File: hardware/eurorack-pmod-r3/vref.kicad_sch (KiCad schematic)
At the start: 6 parts, among them U8 LM4040DBZ-3, U9 TL072

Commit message: rev3/schematic: add PN and footprint for most components
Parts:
- C26: lcsc# (none) -> C110055; mfg# T491A106K020AT -> T491A106K016AT
- C27: lcsc# (none) -> C338036; mfg# (none) -> C1608X7R1E104KT000N
- R33: renamed from R25; lcsc# (none) -> C105881; mfg# (none) -> RC0603FR-07330RL
- RN7: renamed from RN9; footprint Resistor_SMD:R_Cat16-4 -> Resistor_SMD:R_Array_Convex_4x0402; dig# CAT16-1003F4LFCT-ND -> (none); lcsc# (none) -> C326786; mfg# CAT16-1003F4LF -> YC124-FR-07100KL
- U8: dig# 296-LM4040CEM3X-3.0/NOPBCT-ND -> LM4040BIM3-3.0/NOPB; lcsc# (none) -> C139380; mfg# LM4040CEM3X-3.0/NOPB -> LM4040BIM3-3.0/NOPB
- U9: footprint Package_SO:TSSOP-8_4.4x3mm_P0.65mm -> Package_SO:SOIC-8_3.9x4.9mm_P1.27mm; dig# 296-TL072HIPWRCT-ND -> 497-2200-1-ND; lcsc# (none) -> C6961; mfg# TL072HIPWR -> TL072CDT

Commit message: rev3/pcb: preliminary fab outputs and text labels
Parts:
- C26: value 10u -> 10.0uF
- C27: value 100n -> 100nF
- U8: value LM4040DBZ-3 -> LM4040DBZ-3 VREF
- U9: value TL072 -> TL072 OP AMP
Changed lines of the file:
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@@
       (effects (font (size 1.27 1.27)) (justify right))
     )
-    (property "Value" "LM4040DBZ-3" (id 1) (at 100.0252 45.7453 90)
+    (property "Value" "LM4040DBZ-3 VREF" (id 1) (at 100.0252 45.7453 90)
       (effects (font (size 1.27 1.27)) (justify right))
     )
@@
     (in_bom yes) (on_board yes)
     (property "Reference" "U9" (id 0) (at 165.7604 62.865 0))
-    (property "Value" "TL072" (id 1) (at 165.7604 53.34 0))
+    (property "Value" "TL072 OP AMP" (id 1) (at 165.7604 53.34 0))
     (property "Footprint" "Package_SO:SOIC-8_3.9x4.9mm_P1.27mm" (id 2) (at 165.7604 58.42 0)
       (effects (font (size 1.27 1.27)) hide)
@@
     (in_bom yes) (on_board yes)
     (property "Reference" "U9" (id 0) (at 139.0904 60.325 0))
-    (property "Value" "TL072" (id 1) (at 139.0904 50.8 0))
+    (property "Value" "TL072 OP AMP" (id 1) (at 139.0904 50.8 0))
     (property "Footprint" "Package_SO:SOIC-8_3.9x4.9mm_P1.27mm" (id 2) (at 139.0904 55.88 0)
       (effects (font (size 1.27 1.27)) hide)
@@
       (effects (font (size 1.27 1.27)) (justify left))
     )
-    (property "Value" "100n" (id 1) (at 87.3252 46.3866 0)
+    (property "Value" "100nF" (id 1) (at 87.3252 46.3866 0)
       (effects (font (size 1.27 1.27)) (justify left))
     )
@@
     (in_bom yes) (on_board yes)
     (property "Reference" "C26" (id 0) (at 78.4352 42.5704 0))
-    (property "Value" "10u" (id 1) (at 77.1652 45.1104 0))
+    (property "Value" "10.0uF" (id 1) (at 77.1652 45.1104 0))
     (property "Footprint" "Capacitor_Tantalum_SMD:CP_EIA-3216-10_Kemet-I" (id 2) (at 80.9752 45.1104 0)
       (effects (font (size 1.27 1.27)) hide)
@@
       (effects (font (size 1.27 1.27)) (justify right))
     )
-    (property "Value" "TL072" (id 1) (at 212.09 52.8321 0)
-      (effects (font (size 1.27 1.27)) (justify right))
-    )
+    (property "Value" "TL072 OP AMP" (id 1) (at 212.09 52.8321 0)
+      (effects (font (size 1.27 1.27)) (justify right))
+    )

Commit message: try routing with capsense groundfix
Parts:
- added R36 (x2): X.X, Resistor_SMD:R_0402_1005Metric, symbol Device:R
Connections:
- net +3V0_AREF: now also R36.2
- net GND: now also R36.1
- net at RN7.1 (R1.1), RN7.2 (R2.1): now also R36.1, R36.2; no longer U9.3 (+)
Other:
- note added: "VCOM ADJUST"
- note added: "~1.5V"
- note removed: "+1.5V"
- moved on the sheet: C27, RN7A, RN7B

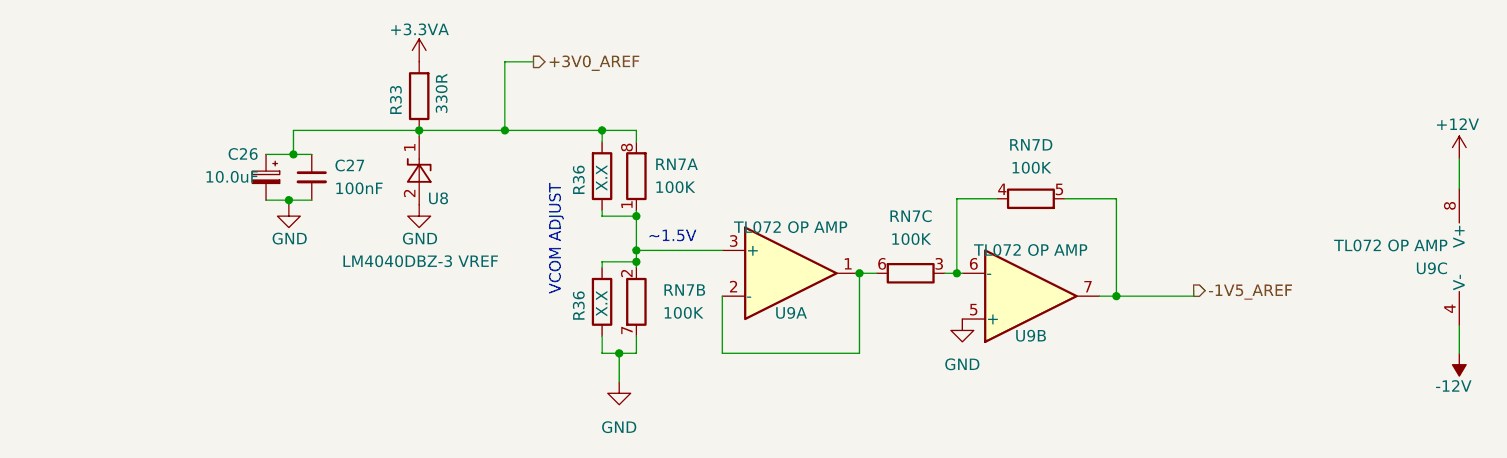
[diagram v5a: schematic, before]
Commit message: Place everything on board, fix some bugs
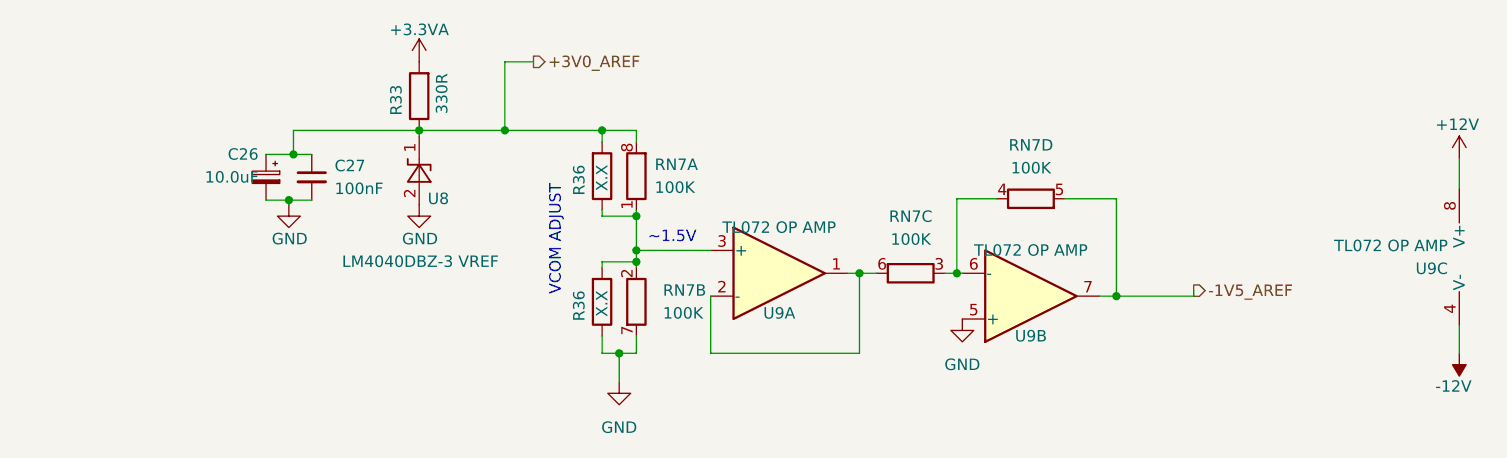
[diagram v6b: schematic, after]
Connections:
- net at R36.1, R36.2, RN7.1 (R1.1)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: now also U9.3 (+)
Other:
- moved on the sheet: U9A
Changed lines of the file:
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@@
+    (stroke (width 0) (type default))
+  )
+  (wire (pts (xy 107.315 32.385) (xy 107.315 40.005))
+    (stroke (width 0) (type default))
+  )
+  (wire (pts (xy 175.26 58.42) (xy 183.8452 58.42))
+    (stroke (width 0) (type default))
+  )
+  (wire (pts (xy 146.7104 64.77) (xy 146.7104 55.88))
+    (stroke (width 0) (type default))
+  )
+  (wire (pts (xy 118.11 41.275) (xy 118.11 40.005))
+    (stroke (width 0) (type default))
+  )
+  (wire (pts (xy 146.7104 55.88) (xy 148.59 55.88))
+    (stroke (width 0) (type default))
+  )
+  (wire (pts (xy 213.36 43.18) (xy 213.36 46.482))
+    (stroke (width 0) (type default))
+  )
+  (wire (pts (xy 118.11 62.865) (xy 118.11 64.77))
+    (stroke (width 0) (type default))
+  )
+  (wire (pts (xy 83.82 40.005) (xy 83.82 42.672))
+    (stroke (width 0) (type default))
+  )
+  (wire (pts (xy 118.11 64.77) (xy 120.015 64.77))
+    (stroke (width 0) (type default))
+  )
+  (wire (pts (xy 97.79 40.005) (xy 97.79 40.64))
+    (stroke (width 0) (type default))
+  )
+  (wire (pts (xy 83.312 47.752) (xy 85.852 47.752))
+    (stroke (width 0) (type default))
+  )
+  (wire (pts (xy 118.11 48.895) (xy 118.11 49.53))
+    (stroke (width 0) (type default))
+  )
+  (wire (pts (xy 107.315 40.005) (xy 118.11 40.005))
+    (stroke (width 0) (type default))
+  )
+  (wire (pts (xy 130.175 64.77) (xy 146.7104 64.77))
+    (stroke (width 0) (type default))
+  )
+  (wire (pts (xy 121.92 40.005) (xy 121.92 41.275))
+    (stroke (width 0) (type default))
+  )
+  (wire (pts (xy 213.36 61.722) (xy 213.36 64.77))
+    (stroke (width 0) (type default))
+  )
+  (wire (pts (xy 183.8452 57.8104) (xy 183.8452 58.42))
+    (stroke (width 0) (type default))
+  )
+  (wire (pts (xy 118.11 40.005) (xy 121.92 40.005))
+    (stroke (width 0) (type default))
+  )
+  (wire (pts (xy 175.26 47.5996) (xy 175.26 58.42))
+    (stroke (width 0) (type default))
+  )
+  (wire (pts (xy 145.415 55.88) (xy 146.7104 55.88))
+    (stroke (width 0) (type default))
+  )
+  (wire (pts (xy 120.015 64.77) (xy 121.92 64.77))
+    (stroke (width 0) (type default))
+  )
+  (wire (pts (xy 173.3804 58.42) (xy 175.26 58.42))
+    (stroke (width 0) (type default))
+  )
+  (wire (pts (xy 121.92 64.77) (xy 121.92 62.865))
     (stroke (width 0) (type default))
   )
@@
     (stroke (width 0) (type default))
   )
-  (wire (pts (xy 107.315 32.385) (xy 107.315 40.005))
-    (stroke (width 0) (type default))
-  )
-  (wire (pts (xy 175.26 58.42) (xy 183.8452 58.42))
-    (stroke (width 0) (type default))
-  )
-  (wire (pts (xy 146.7104 64.77) (xy 146.7104 55.88))
-    (stroke (width 0) (type default))
-  )
-  (wire (pts (xy 118.11 41.275) (xy 118.11 40.005))
-    (stroke (width 0) (type default))
-  )
-  (wire (pts (xy 146.7104 55.88) (xy 148.59 55.88))
-    (stroke (width 0) (type default))
-  )
-  (wire (pts (xy 213.36 43.18) (xy 213.36 46.482))
-    (stroke (width 0) (type default))
-  )
-  (wire (pts (xy 118.11 62.865) (xy 118.11 64.77))
-    (stroke (width 0) (type default))
-  )
-  (wire (pts (xy 83.82 40.005) (xy 83.82 42.672))
-    (stroke (width 0) (type default))
-  )
-  (wire (pts (xy 118.11 64.77) (xy 120.015 64.77))
-    (stroke (width 0) (type default))
-  )
-  (wire (pts (xy 97.79 40.005) (xy 97.79 40.64))
-    (stroke (width 0) (type default))
-  )
-  (wire (pts (xy 83.312 47.752) (xy 85.852 47.752))
-    (stroke (width 0) (type default))
-  )
-  (wire (pts (xy 118.11 48.895) (xy 118.11 49.53))
-    (stroke (width 0) (type default))
-  )
-  (wire (pts (xy 107.315 40.005) (xy 118.11 40.005))
-    (stroke (width 0) (type default))
-  )
-  (wire (pts (xy 131.4704 64.77) (xy 146.7104 64.77))
-    (stroke (width 0) (type default))
-  )
-  (wire (pts (xy 131.445 53.34) (xy 121.92 53.34))
-    (stroke (width 0) (type default))
-  )
-  (wire (pts (xy 121.92 40.005) (xy 121.92 41.275))
-    (stroke (width 0) (type default))
-  )
-  (wire (pts (xy 213.36 61.722) (xy 213.36 64.77))
-    (stroke (width 0) (type default))
-  )
-  (wire (pts (xy 183.8452 57.8104) (xy 183.8452 58.42))
-    (stroke (width 0) (type default))
-  )
-  (wire (pts (xy 118.11 40.005) (xy 121.92 40.005))
-    (stroke (width 0) (type default))
-  )
-  (wire (pts (xy 175.26 47.5996) (xy 175.26 58.42))
-    (stroke (width 0) (type default))
-  )
-  (wire (pts (xy 120.015 64.77) (xy 121.92 64.77))
-    (stroke (width 0) (type default))
-  )
-  (wire (pts (xy 173.3804 58.42) (xy 175.26 58.42))
-    (stroke (width 0) (type default))
-  )
-  (wire (pts (xy 121.92 64.77) (xy 121.92 62.865))
-    (stroke (width 0) (type default))
-  )
-  (wire (pts (xy 131.4704 58.42) (xy 131.4704 64.77))
+  (wire (pts (xy 130.175 58.42) (xy 130.175 64.77))
     (stroke (width 0) (type default))
   )
@@
     (stroke (width 0) (type default))
   )
+  (wire (pts (xy 121.92 53.34) (xy 130.175 53.34))
+    (stroke (width 0) (type default))
+  )
   (wire (pts (xy 80.772 47.752) (xy 83.312 47.752))
     (stroke (width 0) (type default))
@@
     (stroke (width 0) (type default))
   )
-  (wire (pts (xy 121.92 53.34) (xy 121.92 49.53))
+  (wire (pts (xy 121.92 49.53) (xy 121.92 53.34))
     (stroke (width 0) (type default))
   )
@@
     )
   )
-  (symbol (lib_id "Amplifier_Operational:TL072") (at 139.0904 55.88 0) (unit 1)
-    (in_bom yes) (on_board yes) (dnp no)
-    (property "Reference" "U9" (at 139.0904 60.325 0)
-      (effects (font (size 1.27 1.27)))
-    )
-    (property "Value" "TL072 OP AMP" (at 139.0904 50.8 0)
-      (effects (font (size 1.27 1.27)))
-    )
-    (property "Footprint" "Package_SO:SOIC-8_3.9x4.9mm_P1.27mm" (at 139.0904 55.88 0)
-      (effects (font (size 1.27 1.27)) hide)
-    )
-    (property "Datasheet" "https://www.st.com/content/ccc/resource/technical/document/datasheet/bb/4d/19/24/7d/40/48/a6/CD00000490.pdf/files/CD00000490.pdf/jcr:content/translations/en.CD00000490.pdf" (at 139.0904 55.88 0)
-      (effects (font (size 1.27 1.27)) hide)
-    )
-    (property "dig#" "497-2200-1-ND" (at 139.0904 70.485 0)
-      (effects (font (size 1.27 1.27)) hide)
-    )
-    (property "mfg#" "TL072CDT" (at 139.0904 73.025 0)
-      (effects (font (size 1.27 1.27)) hide)
-    )
-    (property "lcsc#" "C6961" (at 139.0904 55.88 0)
-      (effects (font (size 1.27 1.27)) hide)
-    )
+  (symbol (lib_id "Amplifier_Operational:TL072") (at 137.795 55.88 0) (unit 1)
+    (in_bom yes) (on_board yes) (dnp no)
+    (property "Reference" "U9" (at 137.795 60.325 0)
+      (effects (font (size 1.27 1.27)))
+    )
+    (property "Value" "TL072 OP AMP" (at 137.795 50.8 0)
+      (effects (font (size 1.27 1.27)))
+    )
+    (property "Footprint" "Package_SO:SOIC-8_3.9x4.9mm_P1.27mm" (at 137.795 55.88 0)
+      (effects (font (size 1.27 1.27)) hide)
+    )
+    (property "Datasheet" "https://www.st.com/content/ccc/resource/technical/document/datasheet/bb/4d/19/24/7d/40/48/a6/CD00000490.pdf/files/CD00000490.pdf/jcr:content/translations/en.CD00000490.pdf" (at 137.795 55.88 0)
+      (effects (font (size 1.27 1.27)) hide)
+    )
+    (property "dig#" "497-2200-1-ND" (at 137.795 70.485 0)
+      (effects (font (size 1.27 1.27)) hide)
+    )
+    (property "mfg#" "TL072CDT" (at 137.795 73.025 0)
+      (effects (font (size 1.27 1.27)) hide)
+    )
+    (property "lcsc#" "C6961" (at 137.795 55.88 0)
+      (effects (font (size 1.27 1.27)) hide)
+    )

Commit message: fab: add gerber/pnp for r3.2 sent 3 Oct 23
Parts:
- C26: value 10.0uF -> 22.0uF; dig# 399-18019-1-ND -> (none); lcsc# C110055 -> C782264; mfg# T491A106K016AT -> CA45-A-16V-22uF-K
- R36: value X.X -> 402K; lcsc# (none) -> C327345; mfg# (none) -> RC0402FR-07402KL
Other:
- note added: "402K => ~80.1K (eff) (top) VCOM == 1.66V Value taken by statistics across a lot of AK4619s"
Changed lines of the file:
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@@
     (stroke (width 0) (type default))
+  )
+  (text "402K =>\n~80.1K (eff) (top)\nVCOM == 1.66V\n\nValue taken by statistics across a lot of AK4619s"
+    (at 112.014 69.596 0)
+    (effects (font (size 1.27 1.27)) (justify right bottom))
   )
   (text "~1.5V" (at 123.19 52.705 0)
@@
       (effects (font (size 1.27 1.27)) (justify left))
     )
-    (property "Value" "X.X" (at 118.11 43.815 90)
+    (property "Value" "402K" (at 118.11 42.418 90)
       (effects (font (size 1.27 1.27)) (justify left))
     )
@@
       (effects (font (size 1.27 1.27)) hide)
     )
-    (property "lcsc#" "" (at 118.11 45.085 0)
-      (effects (font (size 1.27 1.27)) hide)
-    )
-    (property "mfg#" "" (at 118.11 45.085 0)
+    (property "lcsc#" "C327345" (at 118.11 45.085 0)
+      (effects (font (size 1.27 1.27)) hide)
+    )
+    (property "mfg#" "RC0402FR-07402KL" (at 118.11 45.085 0)
       (effects (font (size 1.27 1.27)) hide)
     )
@@
       (effects (font (size 1.27 1.27)))
     )
-    (property "Value" "10.0uF" (at 76.962 45.212 0)
+    (property "Value" "22.0uF" (at 76.962 45.212 0)
       (effects (font (size 1.27 1.27)))
     )
@@
       (effects (font (size 1.27 1.27)) hide)
     )
-    (property "Datasheet" "https://datasheet.lcsc.com/lcsc/1810252220_KEMET-T491A106K016AT_C110055.pdf" (at 80.772 45.212 0)
-      (effects (font (size 1.27 1.27)) hide)
-    )
-    (property "dig#" "399-18019-1-ND" (at 78.232 52.832 0)
-      (effects (font (size 1.27 1.27)) hide)
-    )
-    (property "mfg#" "T491A106K016AT" (at 78.232 55.372 0)
-      (effects (font (size 1.27 1.27)) hide)
-    )
-    (property "lcsc#" "C110055" (at 80.772 45.212 0)
-      (effects (font (size 1.27 1.27)) hide)
-    )
+    (property "Datasheet" "" (at 80.772 45.212 0)
+      (effects (font (size 1.27 1.27)) hide)
+    )
+    (property "dig#" "" (at 78.232 52.832 0)
+      (effects (font (size 1.27 1.27)) hide)
+    )
+    (property "mfg#" "CA45-A-16V-22uF-K" (at 78.232 55.372 0)
+      (effects (font (size 1.27 1.27)) hide)
+    )
+    (property "lcsc#" "C782264" (at 80.772 45.212 0)
+      (effects (font (size 1.27 1.27)) hide)
+    )
